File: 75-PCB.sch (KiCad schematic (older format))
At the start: 324 parts, among them J1 AVR-ISP-6, Q1 2N7002, SW1 SW_Push, U1 AT90USB1286-AU, U2 PRTR5V0U2X, Y1 16MHz

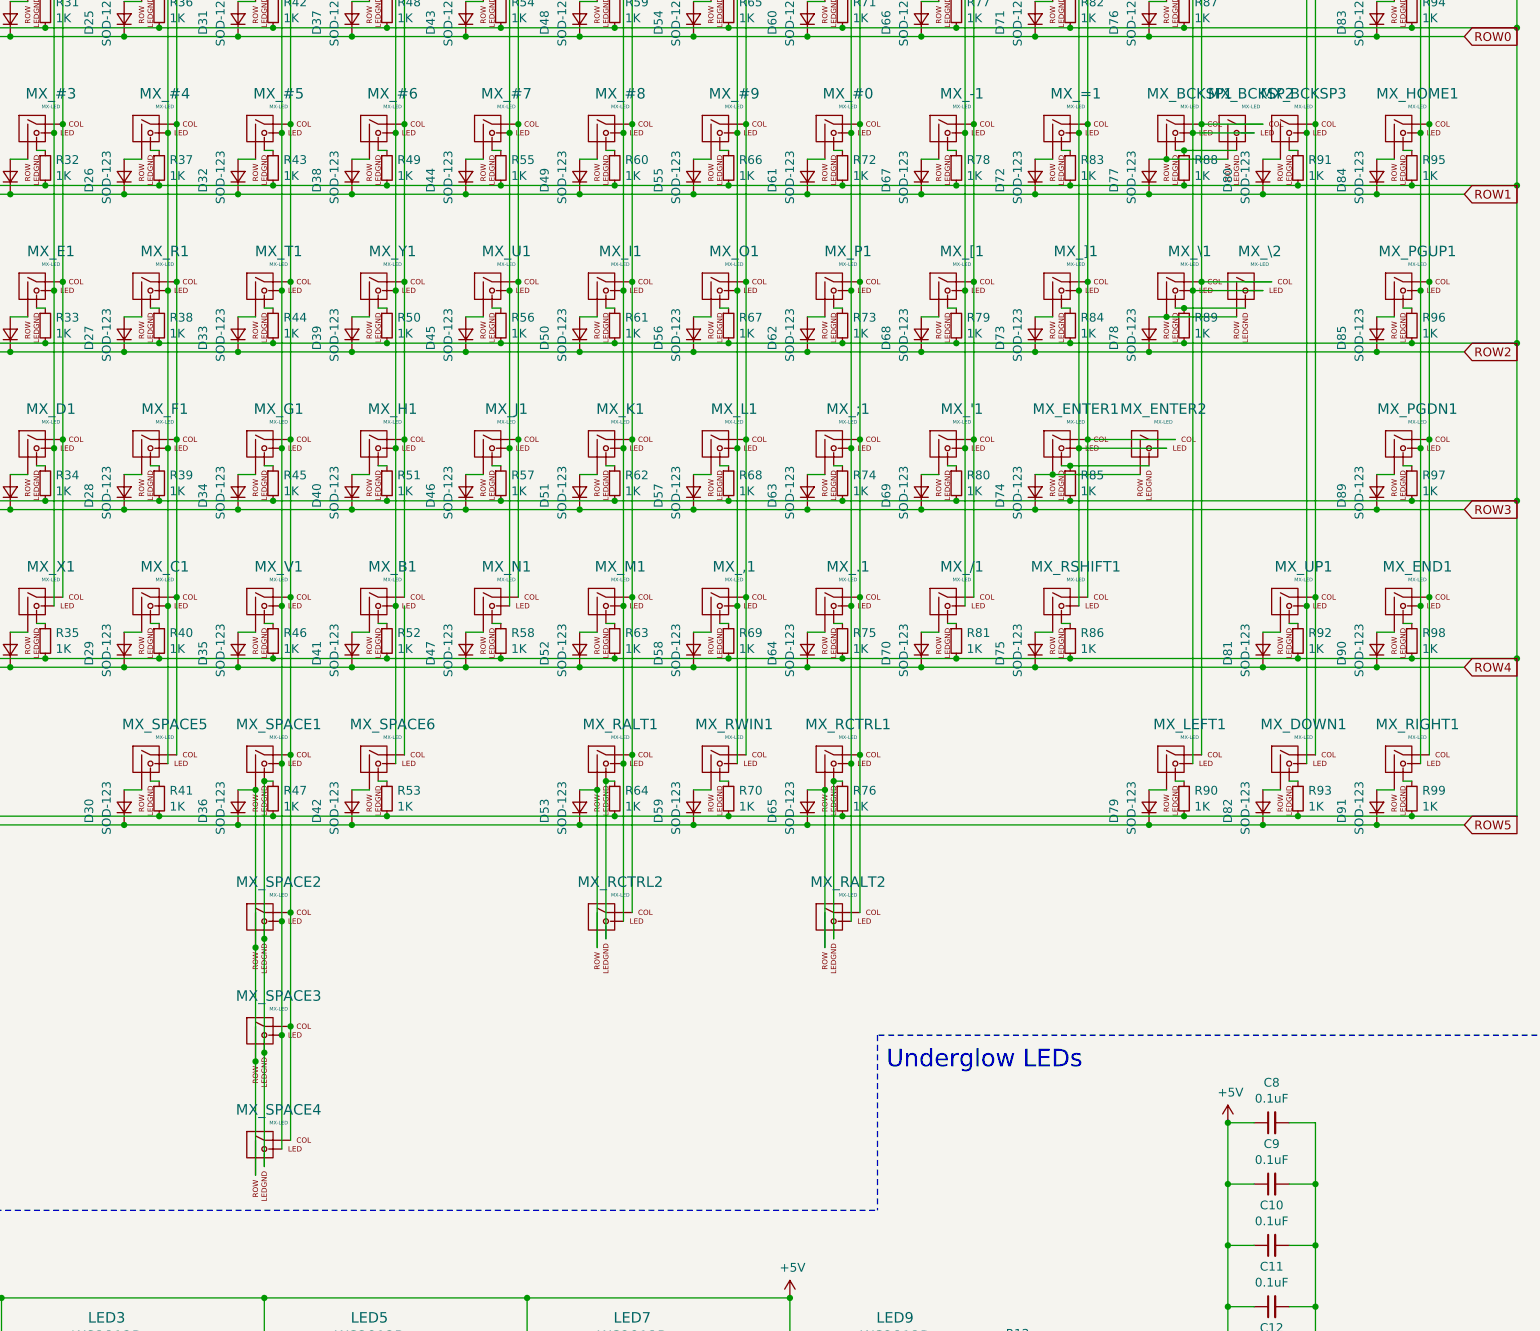
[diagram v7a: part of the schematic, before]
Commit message: Finished switch and LED matrix traces
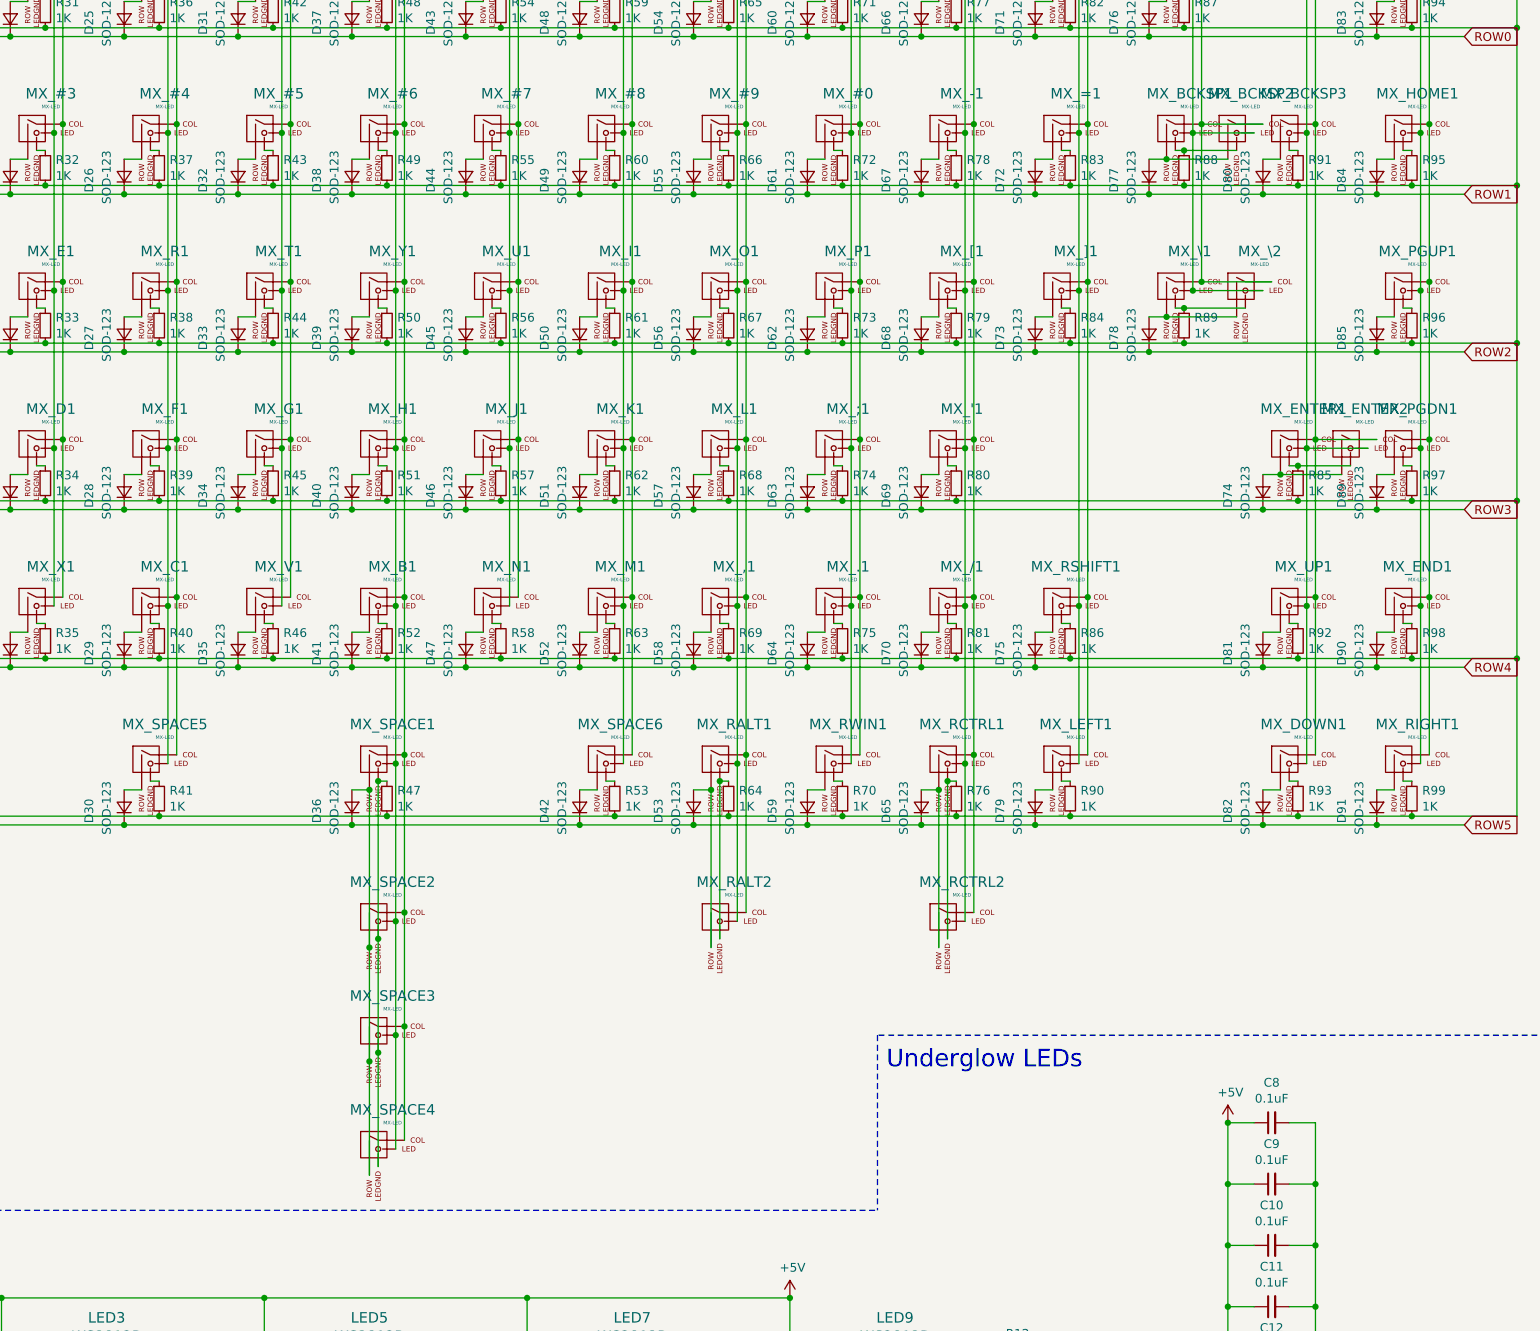
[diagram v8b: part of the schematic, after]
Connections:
- net COL10: now also MX_RWIN1.1 (COL); no longer MX_RALT2.1 (COL), MX_RCTRL1.1 (COL)
- net COL11: now also MX_RCTRL1.1 (COL), MX_RCTRL2.1 (COL)
- net COL12: now also MX_LEFT1.1 (COL); no longer MX_ENTER1.1 (COL), MX_ENTER2.1 (COL)
- net COL13: no longer MX_LEFT1.1 (COL)
- net COL14: now also MX_ENTER1.1 (COL), MX_ENTER2.1 (COL)
- net COL5: no longer MX_SPACE1.1 (COL), MX_SPACE2.1 (COL), MX_SPACE3.1 (COL), MX_SPACE4.1 (COL)
- net COL6: now also MX_SPACE1.1 (COL), MX_SPACE2.1 (COL), MX_SPACE3.1 (COL), MX_SPACE4.1 (COL)
- net COL8: now also MX_SPACE6.1 (COL); no longer MX_RALT1.1 (COL), MX_RCTRL2.1 (COL)
- net COL9: now also MX_RALT1.1 (COL), MX_RALT2.1 (COL); no longer MX_RWIN1.1 (COL)
- net at D53.2 (A), MX_RALT1.2 (ROW): now also MX_RALT2.2 (ROW); no longer MX_RCTRL2.2 (ROW)
- net at MX_RALT1.4 (LEDGND), R64.1: now also MX_RALT2.4 (LEDGND); no longer MX_RCTRL2.4 (LEDGND)
- net at D65.2 (A), MX_RCTRL1.2 (ROW): now also MX_RCTRL2.2 (ROW); no longer MX_RALT2.2 (ROW)
- net at MX_RCTRL1.4 (LEDGND), R76.1: now also MX_RCTRL2.4 (LEDGND); no longer MX_RALT2.4 (LEDGND)
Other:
- moved on the sheet: D36, D42, D53, D59, D65, D74, D79, MX_ENTER1, MX_ENTER2, MX_LEFT1, MX_RALT1, MX_RALT2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
